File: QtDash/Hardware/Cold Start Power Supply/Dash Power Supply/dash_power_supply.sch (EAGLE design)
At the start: 26 parts, among them IC1 LM5060, Q1 IPB042N10N3GATMA1, Q2 IPB042N10N3GATMA1, Q3 600mA/40V

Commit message: bugfix/hardware-revA-issues: 	- added lm3488 5V SEPIC DC/DC converter -- components selected and first draft of layout 	- TODO: select components for input protection and layout the input proectection 	- TODO: add second 5V DC/DC
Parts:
- added C10, C11: 100u, dash_power_supply:CL32A107MPVNNNE
- added C12: 4.7u, digital_dash:CL10A475KL8NRNC
- added C13: .68u, digital_dash:CL10B684KO8NFNC
- added C14, C15: 1n, digital_dash:CL10B102KB8NNWC
- added C6: 100n, digital_dash:CL10B104MB8NNNC
- added C7, C8, C9: 3.3u, dash_power_supply:EEV-FK1K3R3R
- added D10, D11: 3A/10V/280mV, SparkFun-DiscreteSemi:DIODE-SCHOTTKY-BAT60A
- added D9: STPS8H100G-TR, dash_power_supply:STPS8H100G-TR
- added IC2: LM3488, dash_power_supply:LM3488
- added L1: DRQ127-4R7-R, dash_power_supply:DRQ127-4R7-R
- added Q4: BSC027N04LSG, dash_power_supply:BSC027N04LSG
- added R10: 20k, SparkFun-Resistors:20KOHM-0603-1/10W-5%
- added R11: 100R, digital_dash:RC0603JR-07100RL
- added R12: 30.9k 1%, dash_power_supply:RC1206FR-0730K9L
- added R13: 10k 1%, digital_dash:RC0603FR-1010KL
- added R14: 75k, SparkFun-Resistors:75KOHM-0603-1/10W-1%
- added R15: 6mOhm, dash_power_supply:PRL1632-R006-F-T1
- added R16: 270 1%, digital_dash:RC0603FR-07270RL
- added R17: 0, SparkFun-Resistors:0OHM-0603-1/10W
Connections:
- removed net VOUT: D2.C, D3.C, Q2.D, R9.2
- new net 5V: C10.1, C11.1, D11.A, D9.C, R12.2
- new net N$11: Q4.G, R17.2
- new net N$12: C6.1, IC2.VIN, R10.1
- new net N$13: IC2.FB, R12.1, R13.2
- new net N$15: IC2.DR, R17.1
- new net N$16: C15.1, IC2.ISEN, R11.1
- new net N$17: Q4.S, R11.2, R15.2
- new net N$18: C12.1, L1.3, Q4.D
- new net N$19: C12.2, D9.A, L1.4
- new net N$20: C14.1, IC2.COMP, R16.2
- new net N$21: C13.1, R16.1
- new net N$22: IC2.SYNC, R14.2
- new net N$23: D10.C, R5.1
- new net VBATT: C7.+, C8.+, C9.+, D2.C, D3.C, L1.1, Q2.D, R10.2, R9.2
- net GND: now also C10.2, C11.2, C13.2, C14.2, C15.2, C6.2, C7.-, C8.-, C9.-, IC2.AGND, IC2.PGND, L1.2, R13.1, R14.1, R15.1
- net VIN_LM5060: now also D10.A, D11.C; no longer R5.1
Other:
- note added: "Input Protection"

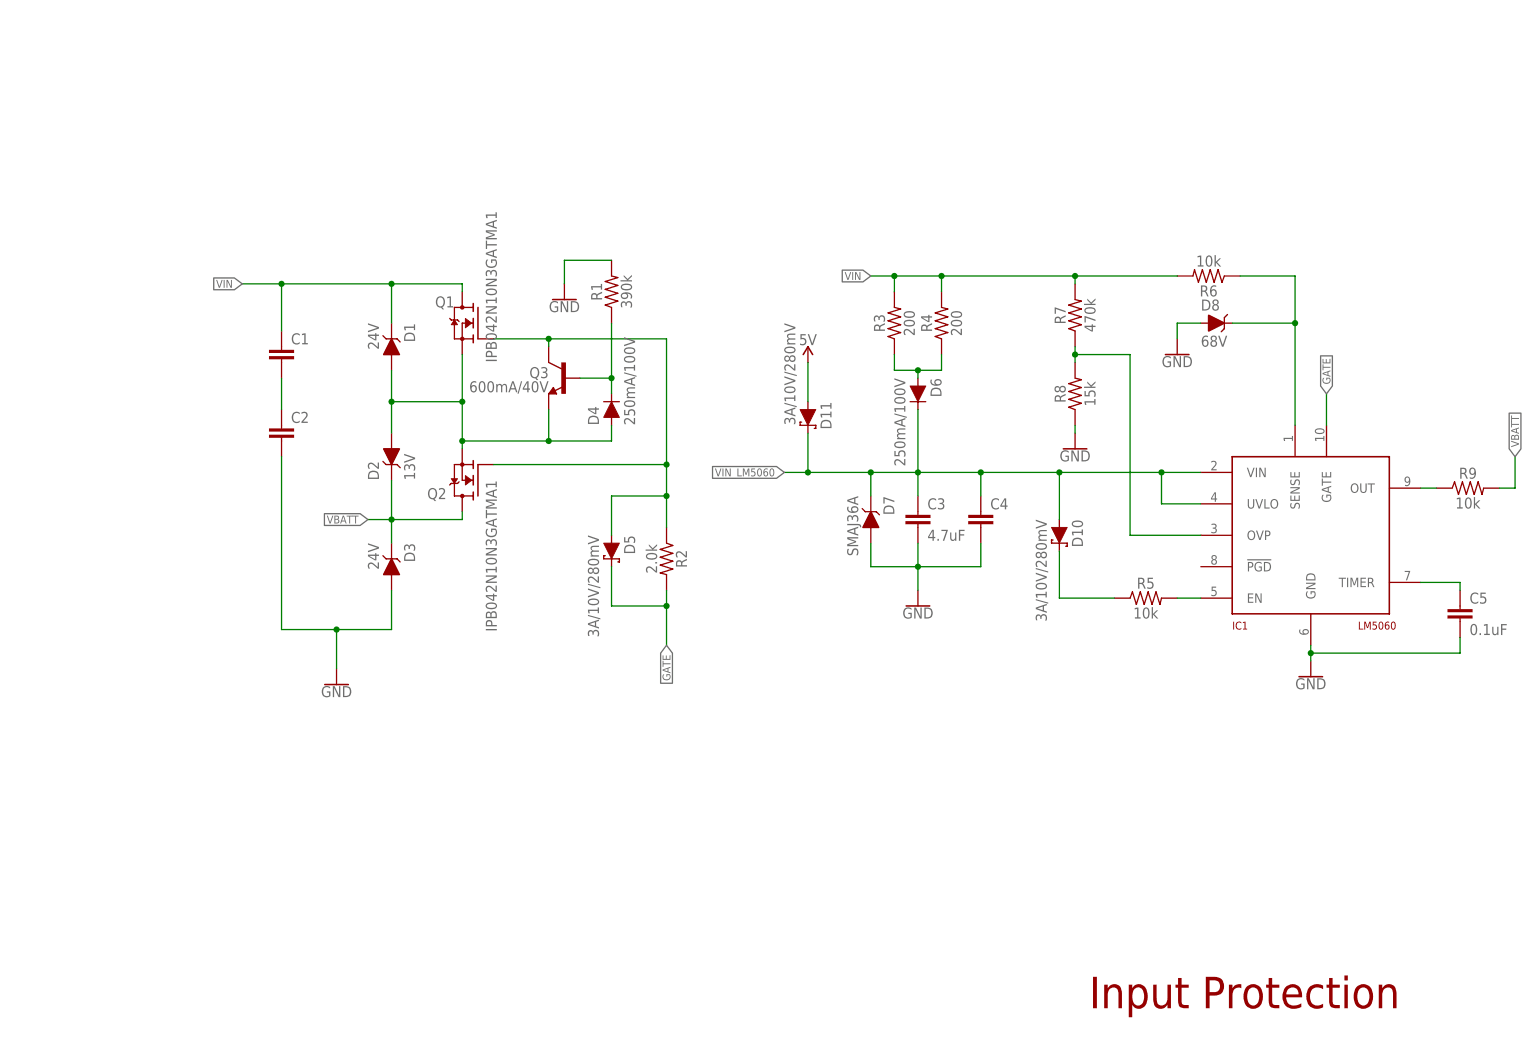
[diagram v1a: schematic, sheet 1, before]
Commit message: bugfix/hardware-revA-issues: 	- first draft of cold start power supply board layout -- passed DRC
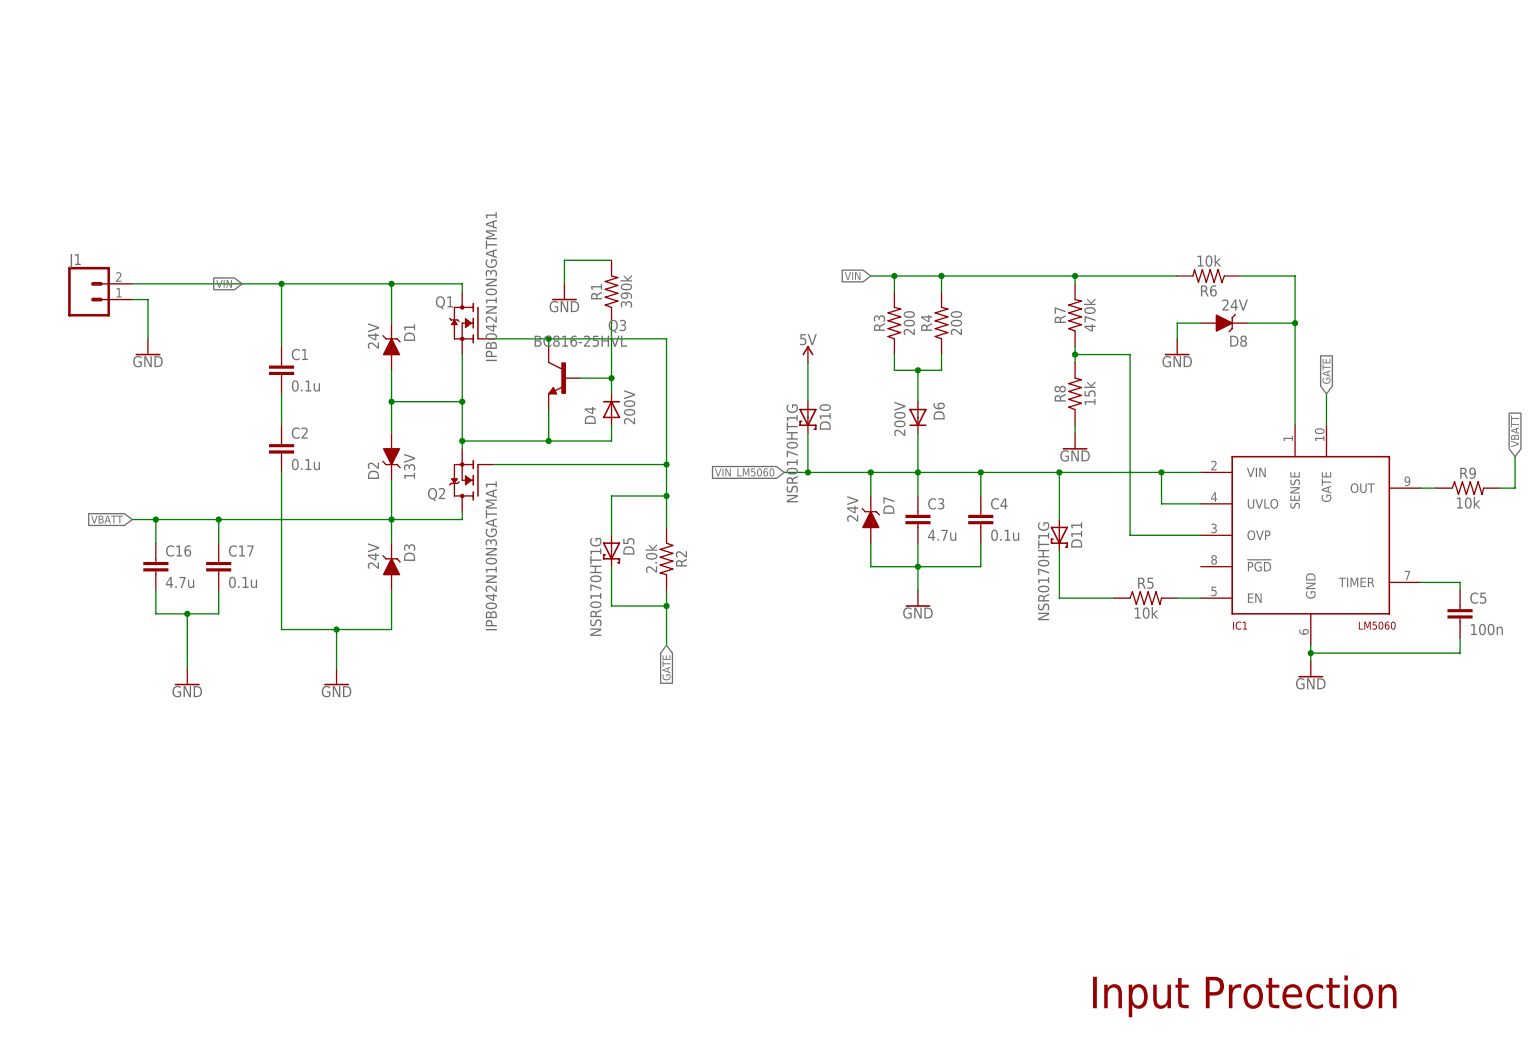
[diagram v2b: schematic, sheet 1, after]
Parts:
- added C16: 4.7u, dash_power_supply:CL32B475KCVZW6E
- added C17: 0.1u, dash_power_supply:CL32B104KCFNNWE
- added J1, J2: (no value), SparkFun-Connectors:CONN_02PTH4
- C1, C2, C4: value (none) -> 0.1u; device SparkFun-Capacitors:CAP-1206 -> dash_power_supply:CL32B104KCFNNWE
- C3: value 4.7uF -> 4.7u; device SparkFun-Capacitors:4.7UF-1206-16V-(+80/-20%) -> dash_power_supply:CL32B475KCVZW6E
- C5: value 0.1uF -> 100n; device SparkFun-Capacitors:0.1UF-0603-100V-10% -> digital_dash:CL10B104MB8NNNC
- D1, D3: device SparkFun-DiscreteSemi:DIODE_TVS_UNI -> dash_power_supply:5.0SMDJ24A
- D10, D11, D5: value 3A/10V/280mV -> NSR0170HT1G; device SparkFun-DiscreteSemi:DIODE-SCHOTTKY-BAT60A -> dash_power_supply:NSR0170HT1G
- D2: device SparkFun-DiscreteSemi:DIODE_TVS_UNI -> dash_power_supply:PTVS13VS1UR,115
- D4, D6: value 250mA/100V -> 200V; device SparkFun-DiscreteSemi:DIODE-BAS16J -> dash_power_supply:ES07B-GS18
- D7: value SMAJ36A -> 24V; device SparkFun-DiscreteSemi:DIODE_TVS_UNI -> dash_power_supply:SZ1SMA24AT3G
- D8: value 68V -> 24V; device SparkFun-DiscreteSemi:DIODE-ZENER-BZX84C15LT3G -> dash_power_supply:SZ1SMA24AT3G
- Q3: value 600mA/40V -> BC816-25HVL; device SparkFun-DiscreteSemi:TRANS_NPN-MMBT2222AL -> dash_power_supply:BC816-25HVL
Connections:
- net N$1 renamed G
- net N$5 renamed VIN_INTERNAL
- net 5V: now also D10.A, J2.1; no longer D11.A
- net GND: now also C16.2, C17.2, J1.1, J2.2
- net N$23: now also D11.C; no longer D10.C
- net VBATT: now also C16.1, C17.1
- net VIN: now also J1.2
- net VIN_LM5060: now also D10.C, D11.A; no longer D10.A, D11.C
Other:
- moved on the sheet: C1, C2, D8
